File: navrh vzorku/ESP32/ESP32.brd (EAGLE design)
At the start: 168.9 x 105.1 mm, 20 parts, among them U1 ESP-WROOM-32

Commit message: funkcni vzorek ESP8266
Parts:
- moved R2 73.4 mm to (12.7, 12.7), turned to 90 degrees
- moved S3 60.2 mm to (10.2, 25.4), turned to 180 degrees
- moved R7 59.1 mm to (16.5, 12.7)
- moved R3 53.6 mm to (49.5, 21.6)
- moved LED1 49.5 mm to (25.4, 10.2), turned to 0 degrees
- moved R1 47.1 mm to (21.6, 36.8)
- moved R4 47.0 mm to (14.0, 39.4)
- moved C1 47.0 mm to (17.8, 31.8)
- moved U$1 47.0 mm to (16.5, 36.8)
- moved C2 45.7 mm to (17.8, 40.6)
- moved MERENI_UBYTKU_NAPETI 45.7 mm to (10.2, 40.6)
- moved READ_WRITE 44.9 mm to (49.5, 43.2)
- moved UARTMODE 44.9 mm to (52.1, 29.2)
- moved NAPAJENI 44.5 mm to (17.8, 47.0)
- moved U1 43.7 mm to (36.8, 39.4)
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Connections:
- net N$3: now also S3.3; no longer S3.4
- net N$5: now also S3.1; no longer S3.2
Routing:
- net N$2: track 85.3 -> 114.9 mm
- net N$5: track 16.9 -> 35.6 mm
- net N$9: track 2.46 -> 20.3 mm
- net N$1: track 23.0 -> 15.8 mm
- net N$3: track 28.7 -> 35.6 mm
- net N$14: track 2.54 -> 8.67 mm
- net N$8: track 16.4 -> 10.6 mm
- net N$13: track 17.8 -> 14.0 mm, vias 1 -> 0
- net N$7: track 6.73 -> 4.19 mm
- net N$6: track 6.27 -> 3.73 mm
- net N$12: track 19.6 -> 17.1 mm
- net N$11: track 19.6 -> 17.1 mm
- net N$16: track 55.9 -> 58.2 mm
- net N$4: track 5.06 -> 3.71 mm
- net N$10: track 7.93 -> 8.45 mm
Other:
- board size 168.9 x 105.1 mm -> 63.5 x 70.8 mm
- board text added: "ESP32 NETIO ovladač"
- board text added: "Milan Jiříček"

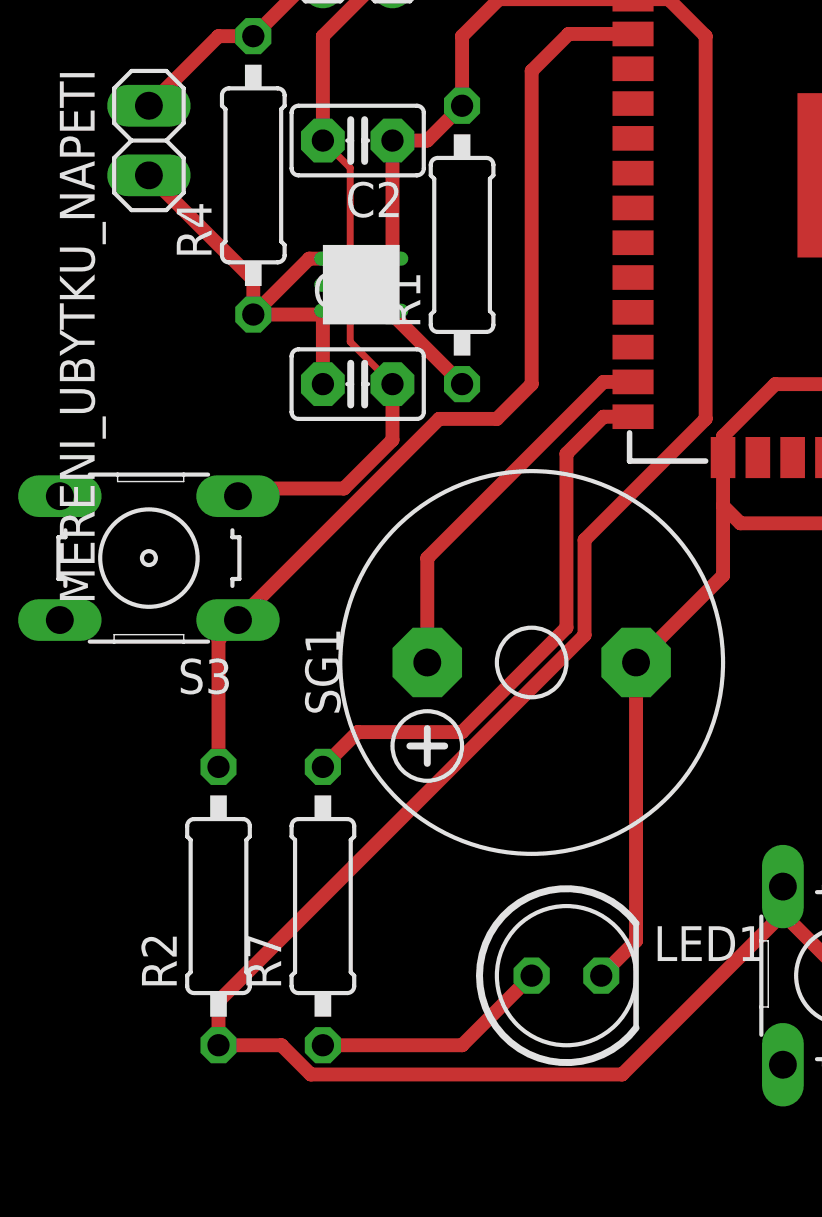
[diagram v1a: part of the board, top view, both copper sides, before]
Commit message: Dokumetace tvorba esp8266 vzorku
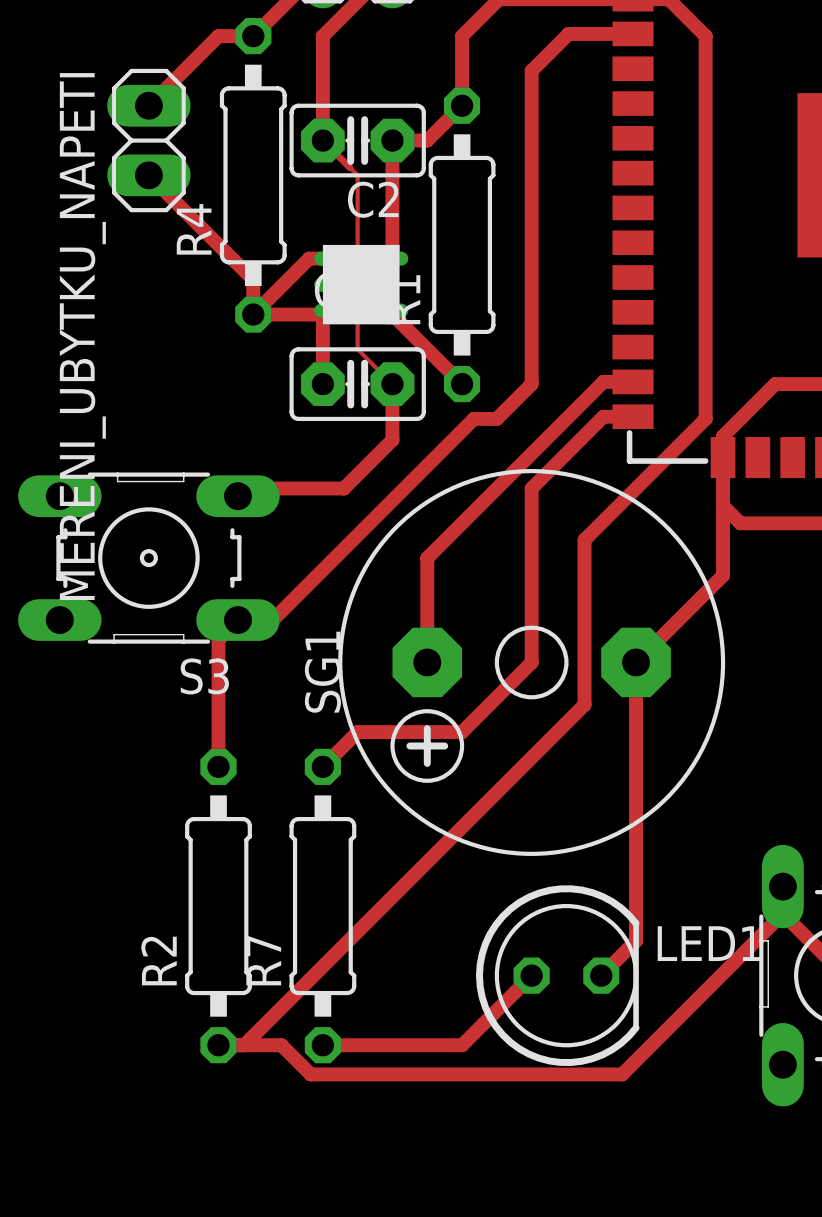
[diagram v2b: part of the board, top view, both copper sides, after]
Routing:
- net N$2: track 114.9 -> 115.5 mm
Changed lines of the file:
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@@
 <drawing>
 <settings>
-<setting alwaysvectorfont="yes"/>
+<setting alwaysvectorfont="no"/>
 <setting verticaltext="up"/>
 </settings>
@@
 <wire x1="16.0681125" y1="6.5532" x2="27.432" y2="6.5532" width="0.508" layer="1"/>
 <wire x1="27.432" y1="6.5532" x2="33.2994" y2="12.4206" width="0.508" layer="1"/>
-<wire x1="26.0604" y1="22.58645" x2="26.0604" y2="26.0604" width="0.508" layer="1"/>
-<wire x1="12.7" y1="7.62" x2="12.7" y2="9.22605" width="0.508" layer="1"/>
-<wire x1="12.7" y1="9.22605" x2="26.0604" y2="22.58645" width="0.508" layer="1"/>
+<wire x1="26.0604" y1="20.04645" x2="26.0604" y2="26.0604" width="0.508" layer="1"/>
+<wire x1="26.0604" y1="20.04645" x2="13.63395" y2="7.62" width="0.508" layer="1"/>
+<wire x1="12.7" y1="7.62" x2="13.63395" y2="7.62" width="0.508" layer="1"/>
 <wire x1="29.13" y1="45.8" x2="27.83" y2="45.8" width="0.508" layer="1"/>
 <wire x1="26.0604" y1="26.0604" x2="30.48" y2="30.48" width="0.508" layer="1"/>
@@
 <wire x1="19.13" y1="47.07" x2="27.83" y2="47.07" width="0.508" layer="1"/>
 <wire x1="16.51" y1="40.64" x2="17.5074" y2="39.6426" width="0.254" layer="1"/>
-<wire x1="17.5074" y1="39.6426" x2="17.5074" y2="35.56" width="0.254" layer="1"/>
-<wire x1="17.5074" y1="35.56" x2="17.5074" y2="33.2926" width="0.254" layer="1"/>
-<wire x1="17.5074" y1="33.2926" x2="19.05" y2="31.75" width="0.254" layer="1"/>
 <wire x1="13.4112" y1="27.6606" x2="13.6906" y2="27.94" width="0.508" layer="1"/>
 <wire x1="13.6906" y1="27.94" x2="17.27785" y2="27.94" width="0.508" layer="1"/>
 <wire x1="19.05" y1="29.71215" x2="19.05" y2="31.75" width="0.508" layer="1"/>
 <wire x1="17.27785" y1="27.94" x2="19.05" y2="29.71215" width="0.508" layer="1"/>
-<wire x1="16.71" y1="35.38" x2="16.89" y2="35.56" width="0.254" layer="1"/>
-<wire x1="16.89" y1="35.56" x2="17.5074" y2="35.56" width="0.254" layer="1"/>
 <wire x1="16.51" y1="40.64" x2="16.51" y2="44.45" width="0.508" layer="1"/>
 <wire x1="16.51" y1="44.45" x2="19.05" y2="46.99" width="0.508" layer="1"/>
+<wire x1="17.5074" y1="39.6426" x2="17.78" y2="39.37" width="0.1524" layer="1"/>
+<wire x1="17.78" y1="39.37" x2="17.78" y2="35.56" width="0.1524" layer="1"/>
+<wire x1="17.78" y1="35.56" x2="17.78" y2="33.02" width="0.1524" layer="1"/>
+<wire x1="17.78" y1="33.02" x2="19.05" y2="31.75" width="0.1524" layer="1"/>
+<wire x1="16.71" y1="35.38" x2="16.89" y2="35.56" width="0.1524" layer="1"/>
+<wire x1="16.89" y1="35.56" x2="17.78" y2="35.56" width="0.1524" layer="1"/>
 </signal>
 <signal name="N$4">
@@
 <wire x1="16.51" y1="17.78" x2="17.78" y2="19.05" width="0.508" layer="1"/>
 <wire x1="17.78" y1="19.05" x2="21.59" y2="19.05" width="0.508" layer="1"/>
-<wire x1="21.59" y1="19.05" x2="25.4" y2="22.86" width="0.508" layer="1"/>
-<wire x1="25.4" y1="22.86" x2="25.4" y2="29.21" width="0.508" layer="1"/>
-<wire x1="25.4" y1="29.21" x2="26.75" y2="30.56" width="0.508" layer="1"/>
+<wire x1="21.59" y1="19.05" x2="24.13" y2="21.59" width="0.508" layer="1"/>
+<wire x1="24.13" y1="21.59" x2="24.13" y2="27.94" width="0.508" layer="1"/>
+<wire x1="24.13" y1="27.94" x2="26.75" y2="30.56" width="0.508" layer="1"/>
 <wire x1="26.75" y1="30.56" x2="27.83" y2="30.56" width="0.508" layer="1"/>
 </signal>
@@
 <wire x1="12.7" y1="17.78" x2="12.7" y2="22.4282" width="0.508" layer="1"/>
 <wire x1="12.7" y1="22.4282" x2="13.4112" y2="23.1394" width="0.508" layer="1"/>
-<wire x1="13.4112" y1="23.1394" x2="20.7518" y2="30.48" width="0.508" layer="1"/>
-<wire x1="20.7518" y1="30.48" x2="22.86" y2="30.48" width="0.508" layer="1"/>
+<wire x1="13.4112" y1="23.1394" x2="14.6812" y2="23.1394" width="0.508" layer="1"/>
+<wire x1="22.0218" y1="30.48" x2="14.6812" y2="23.1394" width="0.508" layer="1"/>
+<wire x1="22.0218" y1="30.48" x2="22.86" y2="30.48" width="0.508" layer="1"/>
 <wire x1="22.86" y1="30.48" x2="24.13" y2="31.75" width="0.508" layer="1"/>
 <wire x1="24.13" y1="31.75" x2="24.13" y2="43.18" width="0.508" layer="1"/>

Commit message: Plosne spoje
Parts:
- R7: value 100k -> 10
- moved READ_WRITE 12.9 mm to (61.4, 48.2)
- moved UARTMODE 10.2 mm to (61.4, 33.2)
- moved C2 9.24 mm to (19.5, 49.7)
- moved NAPAJENI 7.85 mm to (17.0, 54.8)
- moved R1 7.20 mm to (24.6, 43.4)
- moved U$1 6.76 mm to (18.2, 43.4)
- moved U1 6.06 mm to (39.8, 44.6)
- moved C1 5.55 mm to (19.5, 37.0)
- moved S2 5.54 mm to (48.7, 10.3)
- moved SG1 5.00 mm to (27.1, 25.6)
- moved MERENI_UBYTKU_NAPETI 4.08 mm to (9.35, 44.6)
- moved S3 4.08 mm to (9.35, 29.4)
- moved R3 4.06 mm to (52.5, 24.3)
- moved R5 4.06 mm to (48.7, 24.3)
- moved R6 4.06 mm to (41.1, 24.3)
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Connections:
- removed net N$16: LED1.K, R5.2, R6.2, SG1.-, U1.15, UARTMODE.2
- removed net N$3: C1.2, C2.2, NAPAJENI.1, S3.3, U$1.GND, U1.1
- new net GND: C1.2, C2.2, LED1.K, NAPAJENI.1, R5.2, R6.2, S3.3, S3.4, SG1.-, U$1.GND, U1.1, U1.15, UARTMODE.2
- net N$5: now also S3.2
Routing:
- net GND: track 0.00 -> 146.3 mm
- net N$16: track 58.2 -> 0.00 mm
- net N$3: track 35.8 -> 0.00 mm
- net N$2: track 115.5 -> 127.2 mm
- net N$1: track 15.8 -> 25.0 mm
- net N$6: track 3.73 -> 12.7 mm
- net N$7: track 4.19 -> 13.0 mm
- net N$8: track 10.6 -> 18.8 mm
- net N$5: track 35.6 -> 42.0 mm
- net N$11: track 17.1 -> 23.0 mm
- net N$10: track 8.45 -> 13.6 mm
- net N$12: track 17.1 -> 22.2 mm
- net N$9: track 20.3 -> 22.0 mm
- net N$4: track 3.71 -> 5.15 mm
- net N$13: track 14.0 -> 15.3 mm
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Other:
- board size 63.5 x 70.8 mm -> 69.5 x 72.8 mm

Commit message: Finalni verze
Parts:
- removed MERENI_UBYTKU_NAPETI: (no value), pinhead:1X02
- removed R1: 100k, rcl:0207/10
- removed R4: 10, rcl:0207/10
- removed U$1: LDLN030, WT8266:LDLN030
- added C3: 0.1u, capacitor-wima:C2.5-2
- added D1, D2: 1N4004, diode:DO41-10
- added JP1: (no value), pinhead:1X03
- added JP2, JP3: (no value), pinhead:1X02
- added R8: (no value), rcl:0207/10
- C1, C2: value (none) -> 22u
- moved SG1 22.2 mm to (14.1, 7.59)
- moved R2 14.9 mm to (19.6, 29.4), turned to 180 degrees
- moved C1 14.1 mm to (21.0, 51.0), turned to 270 degrees
- moved S3 8.62 mm to (14.7, 22.6), turned to 0 degrees
- moved NAPAJENI 6.71 mm to (20.0, 60.8)
- moved S1 5.83 mm to (43.6, 7.35)
- moved S2 5.83 mm to (53.7, 7.35)
- moved R7 5.39 mm to (24.5, 13.4)
- moved LED1 5.39 mm to (30.4, 6.62)
- moved R3 5.00 mm to (57.5, 24.3)
- moved R5 5.00 mm to (53.7, 24.3)
- moved R6 5.00 mm to (46.1, 24.3)
- moved READ_WRITE 5.00 mm to (66.4, 48.2)
- moved U1 5.00 mm to (44.8, 44.6)
- moved UARTMODE 5.00 mm to (66.4, 33.2)
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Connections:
- removed net N$10: MERENI_UBYTKU_NAPETI.1, NAPAJENI.2, R4.2
- removed net N$4: R1.1, U$1.PG
- removed net N$9: R7.2, U1.14
- new net N$15: D1.C, D2.C, JP1.1, R8.2, U1.8
- new net N$17: D1.A, JP2.1
- new net N$18: D2.A, JP3.2
- new net N$3: JP1.3, R2.2, S3.1, S3.2
- net GND: now also C3.2, R8.1; no longer U$1.GND
- net N$1: now also SG1.+, U1.30; no longer C1.1, MERENI_UBYTKU_NAPETI.2, R4.1, U$1.EN, U$1.IN
- net N$11: now also JP2.2
- net N$12: now also JP3.1
- net N$13: now also R7.2; no longer SG1.+
- net N$2: now also C1.1, C3.1, NAPAJENI.2; no longer R1.2, U$1.OUT
- net N$5: now also JP1.2; no longer R2.2, S3.1, S3.2
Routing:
- net N$1: track 25.0 -> 64.3 mm, vias 0 -> 2
- net N$12: track 22.2 -> 58.5 mm
- net N$15: track 0.00 -> 35.0 mm
- net N$17: track 0.00 -> 29.3 mm
- net N$18: track 0.00 -> 22.1 mm
- net N$9: track 22.0 -> 0.00 mm
- net N$3: track 0.00 -> 21.6 mm
- net N$5: track 42.0 -> 24.8 mm
- net N$13: track 15.3 -> 30.3 mm
- net N$10: track 13.6 -> 0.00 mm
- net N$11: track 23.0 -> 35.6 mm
- net GND: track 146.3 -> 158.8 mm
- net N$2: track 127.2 -> 134.5 mm
- net N$8: track 18.8 -> 24.1 mm
- net N$4: track 5.15 -> 0.00 mm
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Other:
- board size 69.5 x 72.8 mm -> 76.5 x 85.8 mm
